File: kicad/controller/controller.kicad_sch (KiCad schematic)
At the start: 34 parts, among them J1 Conn_02x04_Top_Bottom, SW0 1825910-6, SW2 1825910-6, SW4 1825910-6, SW6 1825910-6, U1 MCP3008, U2 MCP23S08T-E/SO

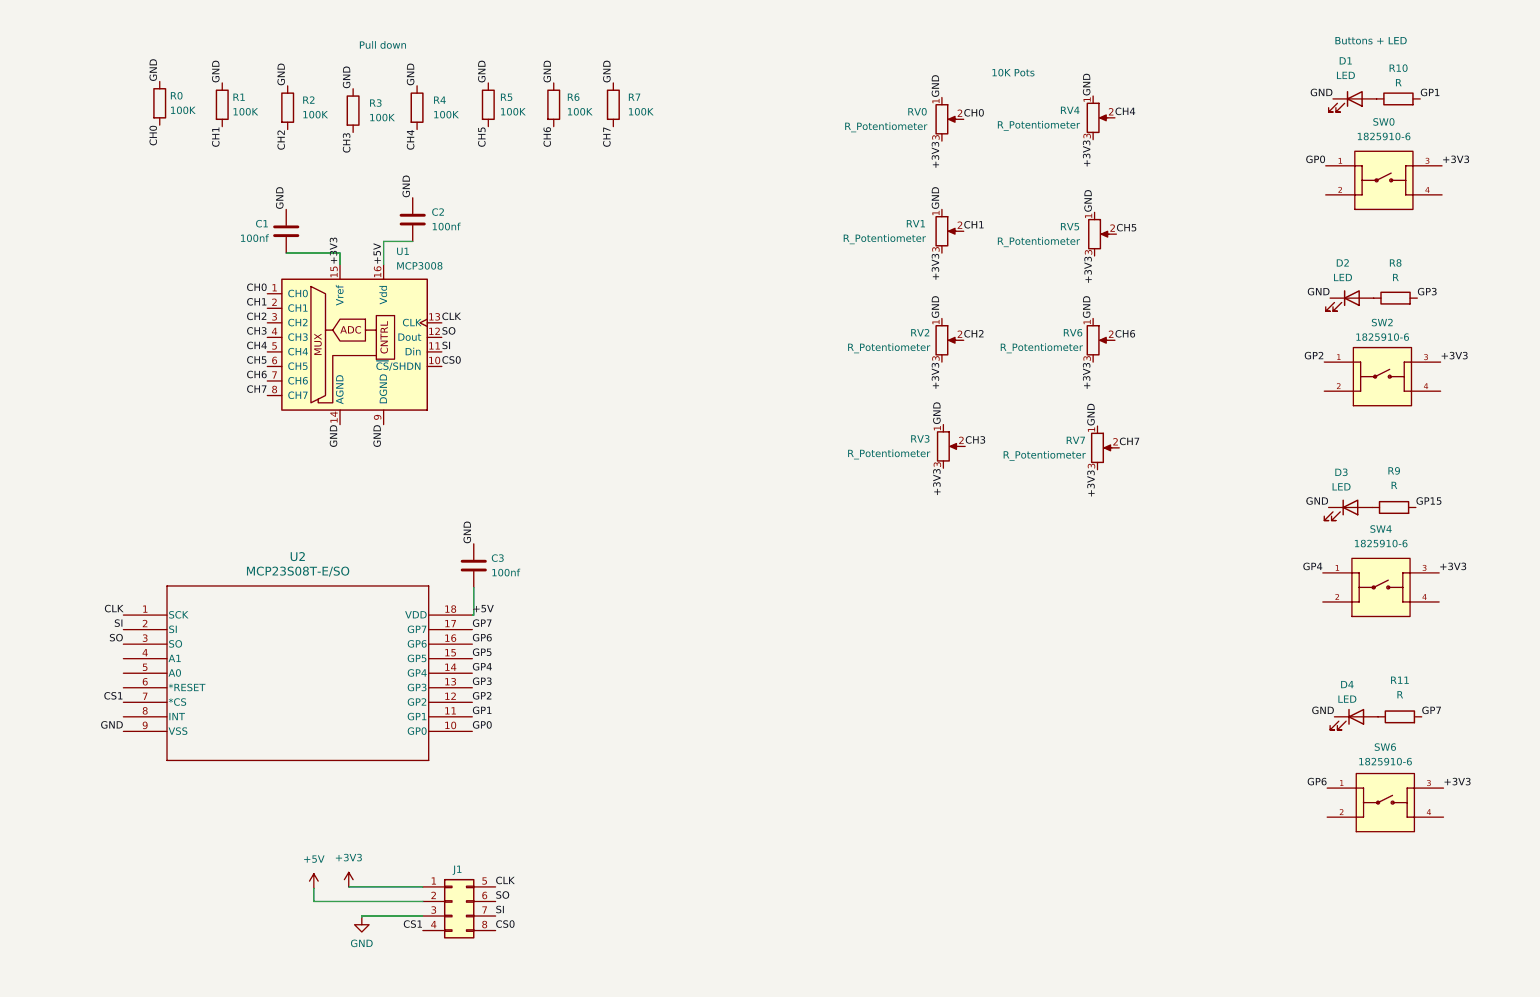
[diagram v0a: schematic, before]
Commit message: tweak metronome and make a LED blink
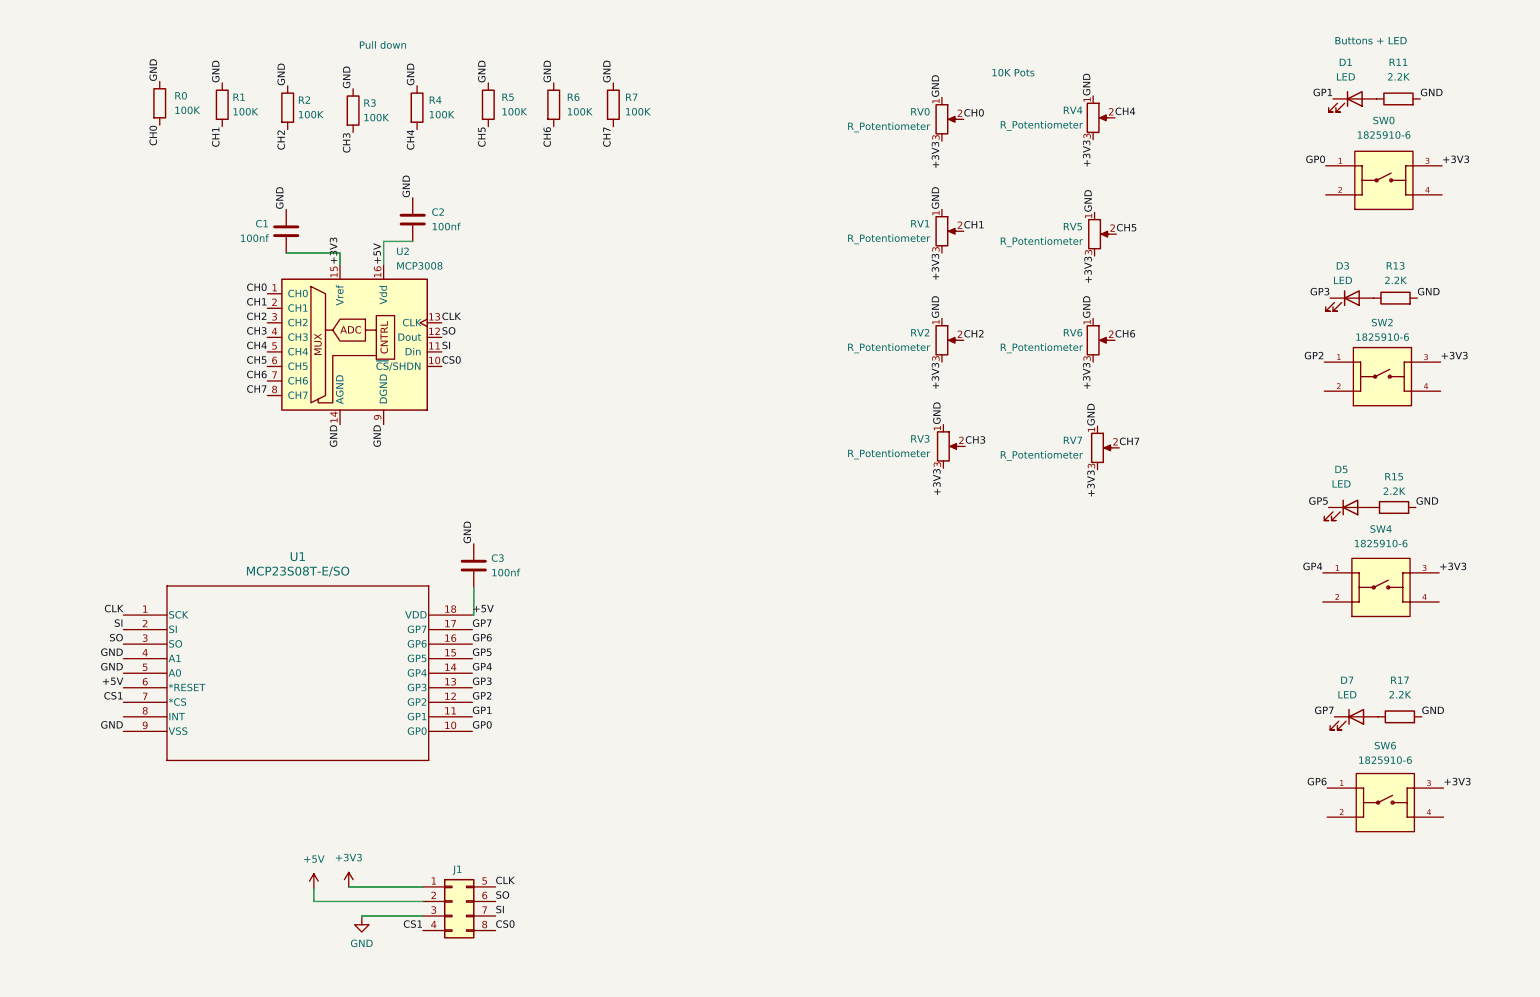
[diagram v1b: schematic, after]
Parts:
- R11: renamed from R10; value R -> 2.2K
- R13: renamed from R8; value R -> 2.2K
- R15: renamed from R9; value R -> 2.2K
- R17: renamed from R11; value R -> 2.2K
- renumbered D2 to D3, D3 to D5, D4 to D7, U2 to U1, U1 to U2
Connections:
- net GP15 is gone; now on net GND: R15.2
- net +5V: now also U1.6 (*RESET)
- net GND: now also R11.2, R13.2, R17.2, U1.4 (A1), U1.5 (A0); no longer D1.1 (K), D3.1 (K), D5.1 (K), D7.1 (K)
- net GP1: now also D1.1 (K); no longer R11.2
- net GP3: now also D3.1 (K); no longer R13.2
- net GP5: now also D5.1 (K)
- net GP7: now also D7.1 (K); no longer R17.2

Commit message: start adding mcp23s08 gpio extender
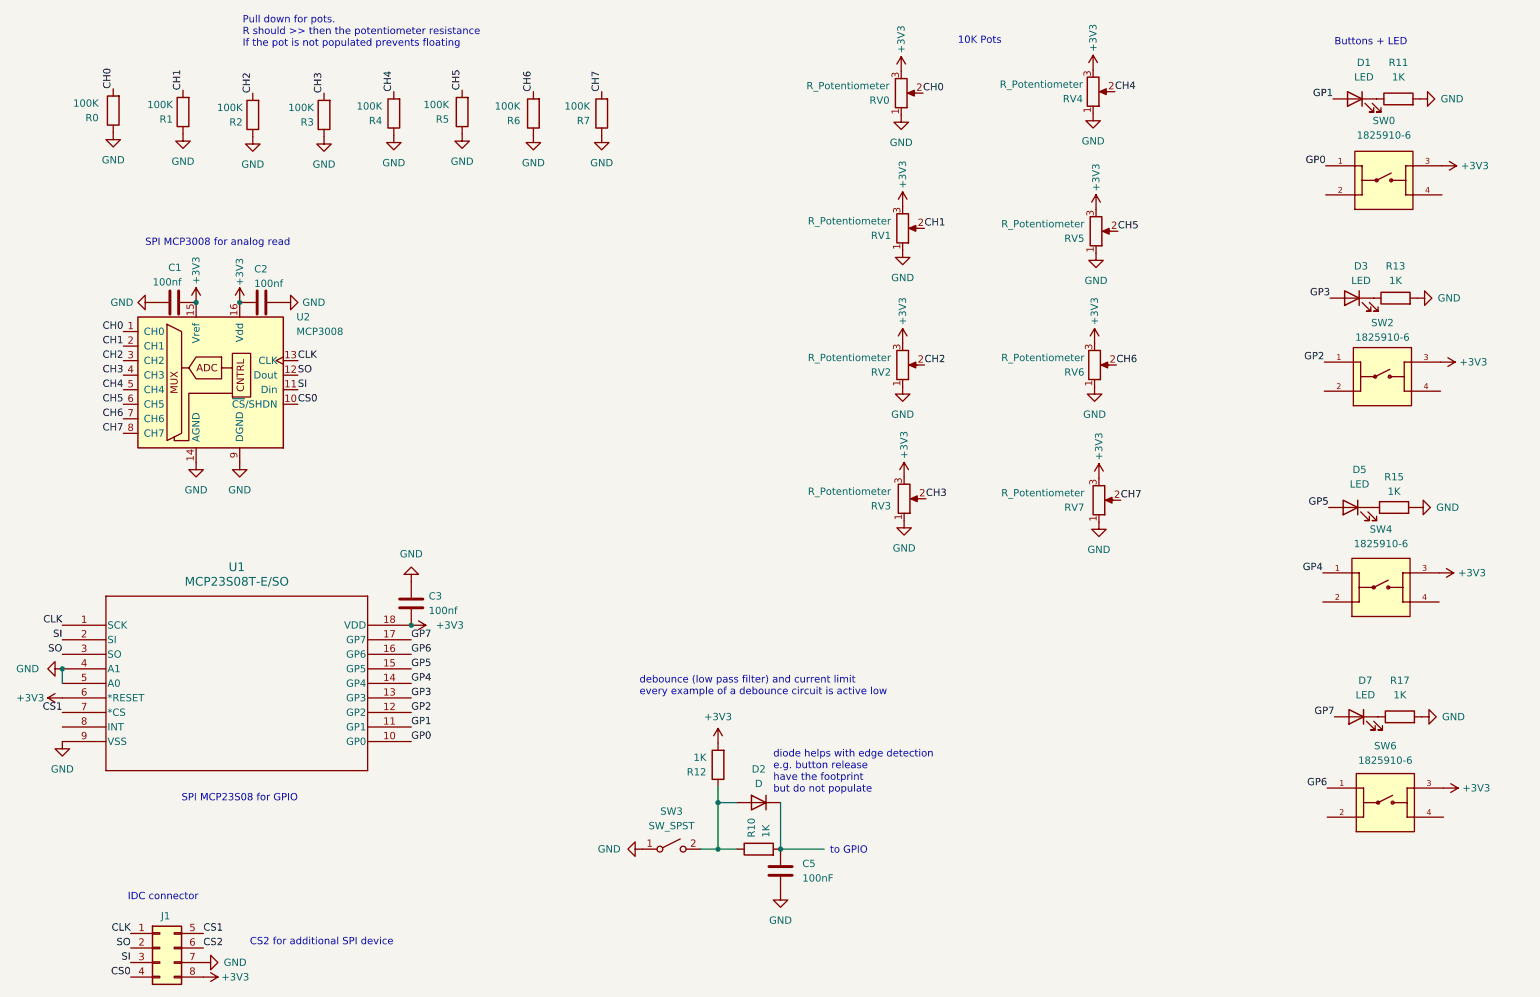
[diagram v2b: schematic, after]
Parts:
- added C5: 100nF, symbol Device:C
- added D2: D, symbol Device:D
- added R10, R12: 1K, symbol Device:R
- added SW3: SW_SPST, symbol Switch:SW_SPST
- R11, R13, R15, R17: value 2.2K -> 1K
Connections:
- net +3V3: now also C2.2, C3.2, J1.8 (Pin_8), U1.18 (VDD), U1.6 (*RESET), U2.16 (Vdd), R12.2; no longer J1.1 (Pin_1)
- net CLK: now also J1.1 (Pin_1); no longer J1.5 (Pin_5)
- net CS0: now also J1.4 (Pin_4); no longer J1.8 (Pin_8)
- net CS1: now also J1.5 (Pin_5); no longer J1.4 (Pin_4)
- net GND: now also J1.7 (Pin_7), C5.2, SW3.1 (A); no longer J1.3 (Pin_3)
- net GP1: now also D1.2 (A); no longer D1.1 (K)
- net GP3: now also D3.2 (A); no longer D3.1 (K)
- net GP5: now also D5.2 (A); no longer D5.1 (K)
- net GP7: now also D7.2 (A); no longer D7.1 (K)
- net SI: now also J1.3 (Pin_3); no longer J1.7 (Pin_7)
- net SO: now also J1.2 (Pin_2); no longer J1.6 (Pin_6)
- net at R13.1: now also D3.1 (K); no longer D3.2 (A)
- net at R15.1: now also D5.1 (K); no longer D5.2 (A)
- net at R11.1: now also D1.1 (K); no longer D1.2 (A)
- net at R17.1: now also D7.1 (K); no longer D7.2 (A)
- removed net +5V: C2.2, C3.2, J1.2 (Pin_2), U1.18 (VDD), U1.6 (*RESET), U2.16 (Vdd)
- new net: C5.1, D2.1 (K), R10.2
- new net: D2.2 (A), R10.1, R12.1, SW3.2 (B)
- new net CS2: J1.6 (Pin_6)
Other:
- note added: "CS2 for additional SPI device"
- note added: "IDC connector"
- note added: "Pull down for pots. R should >> then the potentiometer resistance If the pot is not populated prevents floating"
- note added: "SPI MCP23S08 for GPIO"
- note added: "SPI MCP3008 for analog read"
- note added: "debounce (low pass filter) and current limit every example of a debounce circuit is active low"
- note added: "diode helps with edge detection e.g. button release have the footprint but do not populate"
- note added: "to GPIO"
- note removed: "Pull down"
- title: (none) -> pico-synth-controller
- moved on the sheet: C1, C2, C3, D1, D3, D5, D7, J1, R0, R1, R2, R3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

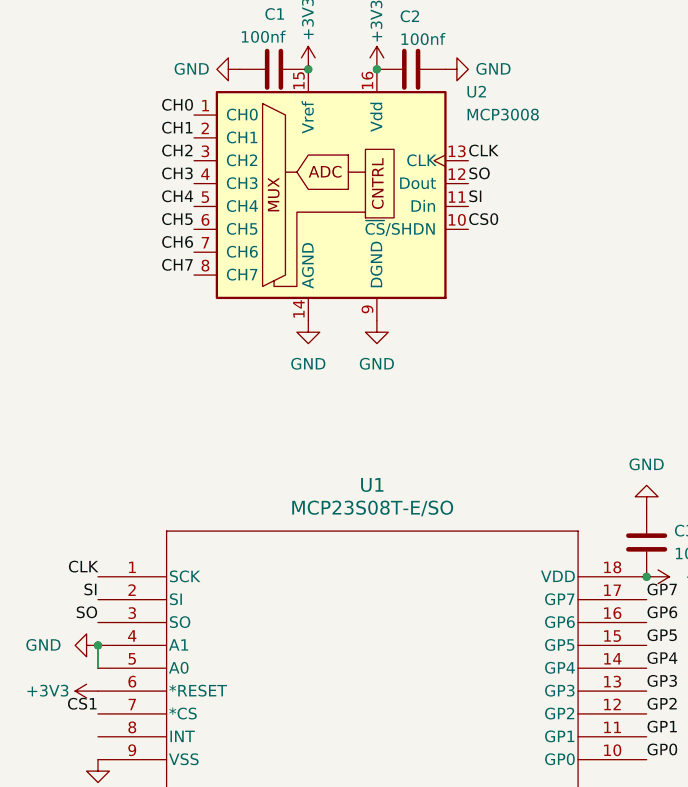
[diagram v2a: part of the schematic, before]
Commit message: fix side-set logic - bool is NOT a char!
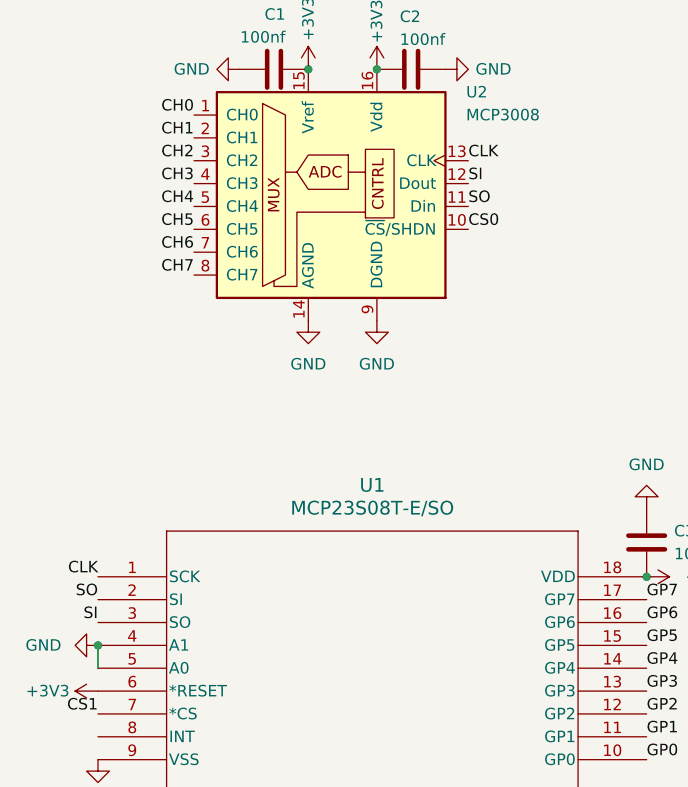
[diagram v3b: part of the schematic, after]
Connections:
- net SI: now also U1.3 (SO), U2.12 (Dout); no longer U1.2 (SI), U2.11 (Din)
- net SO: now also U1.2 (SI), U2.11 (Din); no longer U1.3 (SO), U2.12 (Dout)
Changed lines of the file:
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@@
     (effects (font (size 1.27 1.27)) (justify left bottom))
-  )
-  (label "SO" (at 23.622 124.968 180) (fields_autoplaced)
-    (effects (font (size 1.27 1.27)) (justify right bottom))
   )
   (label "CLK" (at 35.56 173.736 180) (fields_autoplaced)
@@
   )
   (label "GP7" (at 84.582 122.428 0) (fields_autoplaced)
-    (effects (font (size 1.27 1.27)) (justify left bottom))
-  )
-  (label "SI" (at 64.77 78.74 0) (fields_autoplaced)
     (effects (font (size 1.27 1.27)) (justify left bottom))
   )
@@
     (effects (font (size 1.27 1.27)) (justify left bottom))
   )
-  (label "SO" (at 64.77 76.2 0) (fields_autoplaced)
-    (effects (font (size 1.27 1.27)) (justify left bottom))
+  (label "CH0" (at 34.29 68.58 180) (fields_autoplaced)
+    (effects (font (size 1.27 1.27)) (justify right bottom))
   )
-  (label "CH0" (at 34.29 68.58 180) (fields_autoplaced)
+  (label "SO" (at 23.622 122.428 180) (fields_autoplaced)
     (effects (font (size 1.27 1.27)) (justify right bottom))
   )
@@
     (effects (font (size 1.27 1.27)) (justify right bottom))
   )
+  (label "SI" (at 64.77 76.2 0) (fields_autoplaced)
+    (effects (font (size 1.27 1.27)) (justify left bottom))
+  )
   (label "CH7" (at 117.856 26.67 90) (fields_autoplaced)
     (effects (font (size 1.27 1.27)) (justify left bottom))
   )
   (label "GP6" (at 244.602 148.336 180) (fields_autoplaced)
-    (effects (font (size 1.27 1.27)) (justify right bottom))
-  )
-  (label "SI" (at 23.622 122.428 180) (fields_autoplaced)
     (effects (font (size 1.27 1.27)) (justify right bottom))
   )
@@
     (effects (font (size 1.27 1.27)) (justify right bottom))
   )
+  (label "SO" (at 64.77 78.74 0) (fields_autoplaced)
+    (effects (font (size 1.27 1.27)) (justify left bottom))
+  )
   (label "CH2" (at 56.896 26.924 90) (fields_autoplaced)
     (effects (font (size 1.27 1.27)) (justify left bottom))
@@
     (effects (font (size 1.27 1.27)) (justify left bottom))
   )
+  (label "SI" (at 23.622 124.968 180) (fields_autoplaced)
+    (effects (font (size 1.27 1.27)) (justify right bottom))
+  )
   (label "GP1" (at 84.582 137.668 0) (fields_autoplaced)
